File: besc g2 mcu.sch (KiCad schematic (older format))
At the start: 34 parts, among them U8 STM32F405RGTx, Y1 MCSJK-7I-8.00-18-10-60-B-10

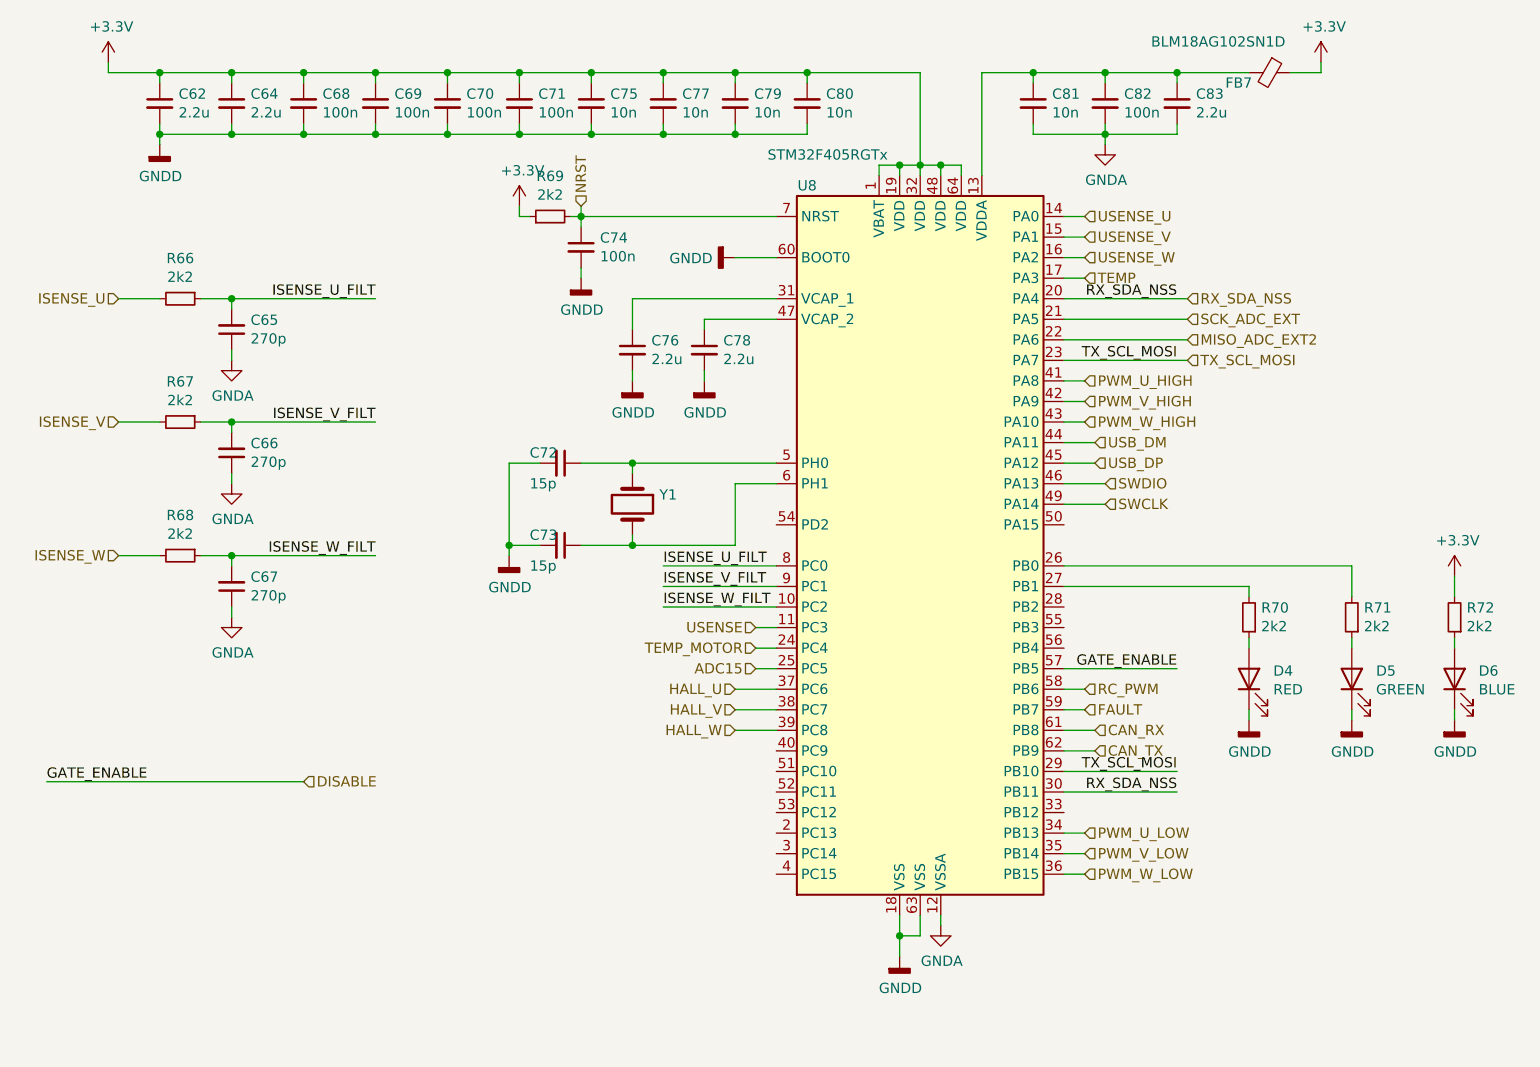
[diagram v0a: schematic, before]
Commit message: Added brakes, i2c
Signed-off-by: manianac <manianac@gmail.com>
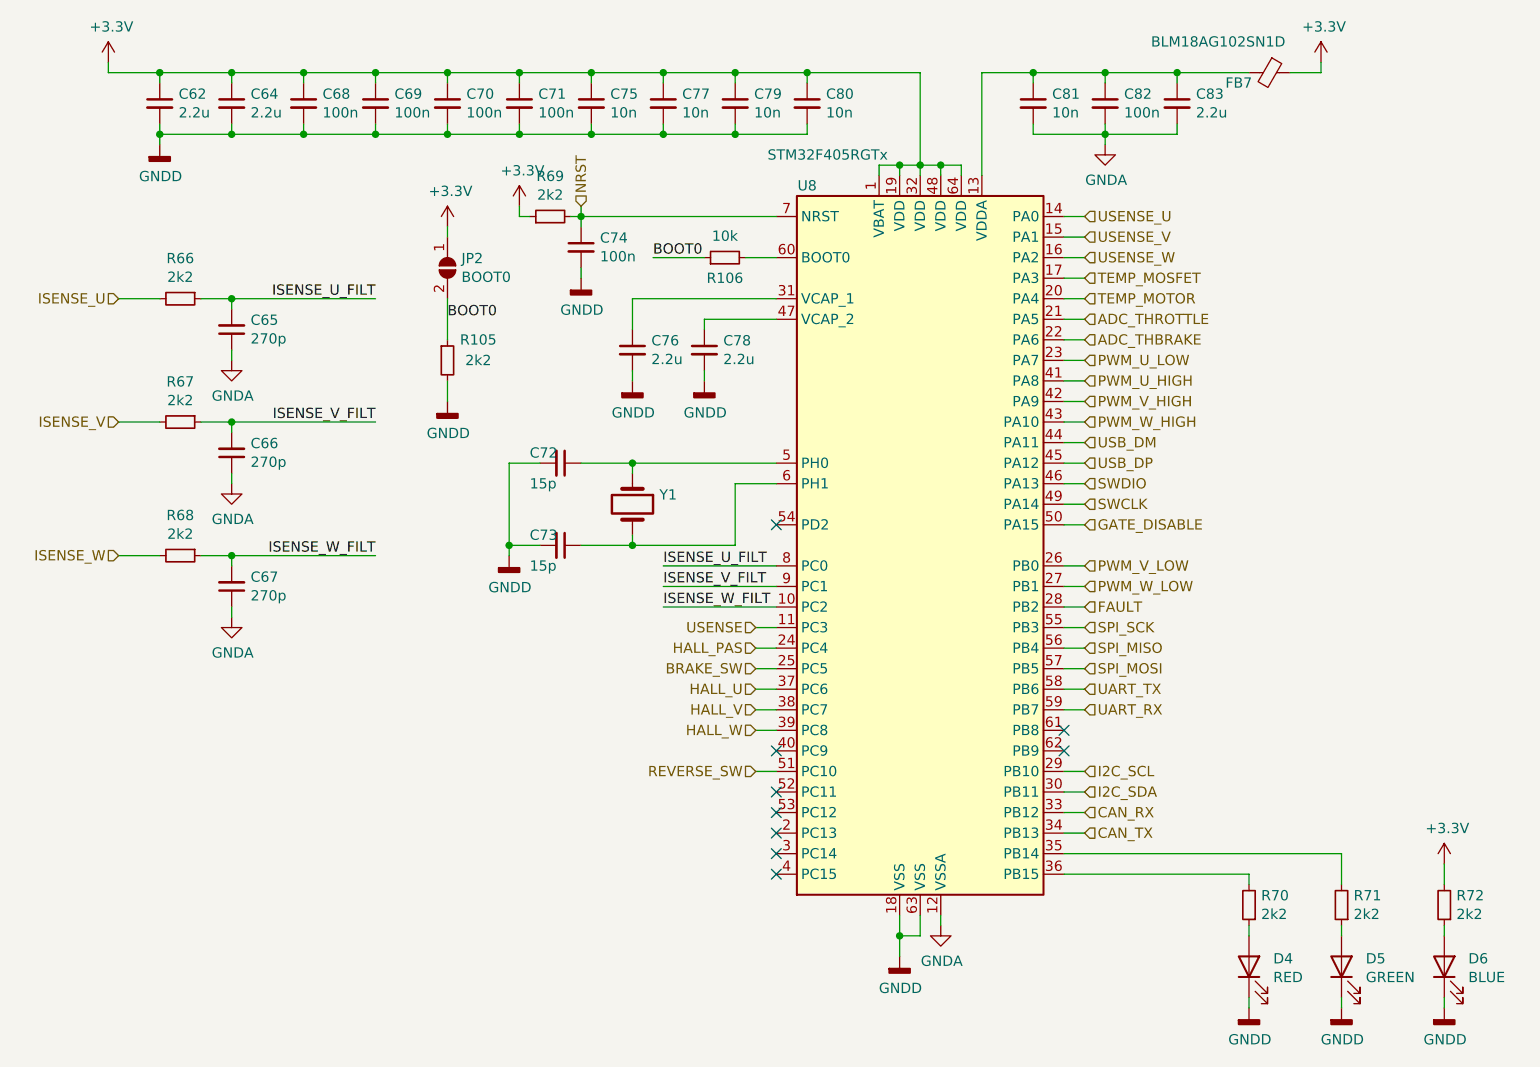
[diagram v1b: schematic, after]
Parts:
- added JP2: BOOT0, Jumper:SolderJumper-2_P1.3mm_Open_RoundedPad1.0x1.5mm, symbol Jumper:SolderJumper_2_Open
- added R105: 2k2, Resistor_SMD:R_0603_1608Metric, symbol Device:R_Small
- added R106: 10k, Resistor_SMD:R_0603_1608Metric, symbol Device:R_Small
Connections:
- net +3V3: now also JP2.1 (A)
- net CAN_RX: now also U8.33 (PB12); no longer U8.61 (PB8)
- net CAN_TX: now also U8.34 (PB13); no longer U8.62 (PB9)
- net FAULT: now also U8.28 (PB2); no longer U8.59 (PB7)
- net GNDD: now also R105.2; no longer U8.60 (BOOT0)
- net PWM_U_LOW: now also U8.23 (PA7); no longer U8.34 (PB13)
- net PWM_V_LOW: now also U8.26 (PB0); no longer U8.35 (PB14)
- net PWM_W_LOW: now also U8.27 (PB1); no longer U8.36 (PB15)
- net TEMP_MOTOR: now also U8.20 (PA4); no longer U8.24 (PC4)
- net at R71.2: now also U8.35 (PB14); no longer U8.26 (PB0)
- net at R70.2: now also U8.36 (PB15); no longer U8.27 (PB1)
- net GATE_DISABLE: now reaches U8.50 (PA15)
- net REVERSE_SW: now reaches U8.51 (PC10)
- net SPI_SCK: now reaches U8.55 (PB3)
- net SPI_MISO: now reaches U8.56 (PB4)
- net ADC15 renamed BRAKE_SW
- net DISABLE renamed SPI_MOSI
- net MISO_ADC_EXT2 renamed ADC_THBRAKE
- net RC_PWM renamed UART_TX
- net RX_SDA_NSS renamed I2C_SDA
- net I2C_SDA: no longer U8.20 (PA4)
- net SCK_ADC_EXT renamed ADC_THROTTLE
- net TEMP renamed TEMP_MOSFET
- net TX_SCL_MOSI renamed I2C_SCL
- net I2C_SCL: no longer U8.23 (PA7)
- new net: R106.2, U8.60 (BOOT0)
- new net BOOT0: JP2.2 (B), R105.1, R106.1
- new net HALL_PAS: U8.24 (PC4)
- new net UART_RX: U8.59 (PB7)
- no-connect marks 0 -> 9
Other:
- moved on the sheet: D4, D5, D6, R70, R71, R72
